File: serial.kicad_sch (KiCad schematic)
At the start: 66 parts, among them IC3 ILD217T, IC4 ILD217T, U14 NCP1117-3.3_SOT223, U15 NCP1117-3.3_SOT223, U16 SP3485EN, U17 NCP1117-3.3_SOT223, U4 ADuM1201AR, U5 ADuM1201AR, U6 ADuM1201AR, U8 SP3485EN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

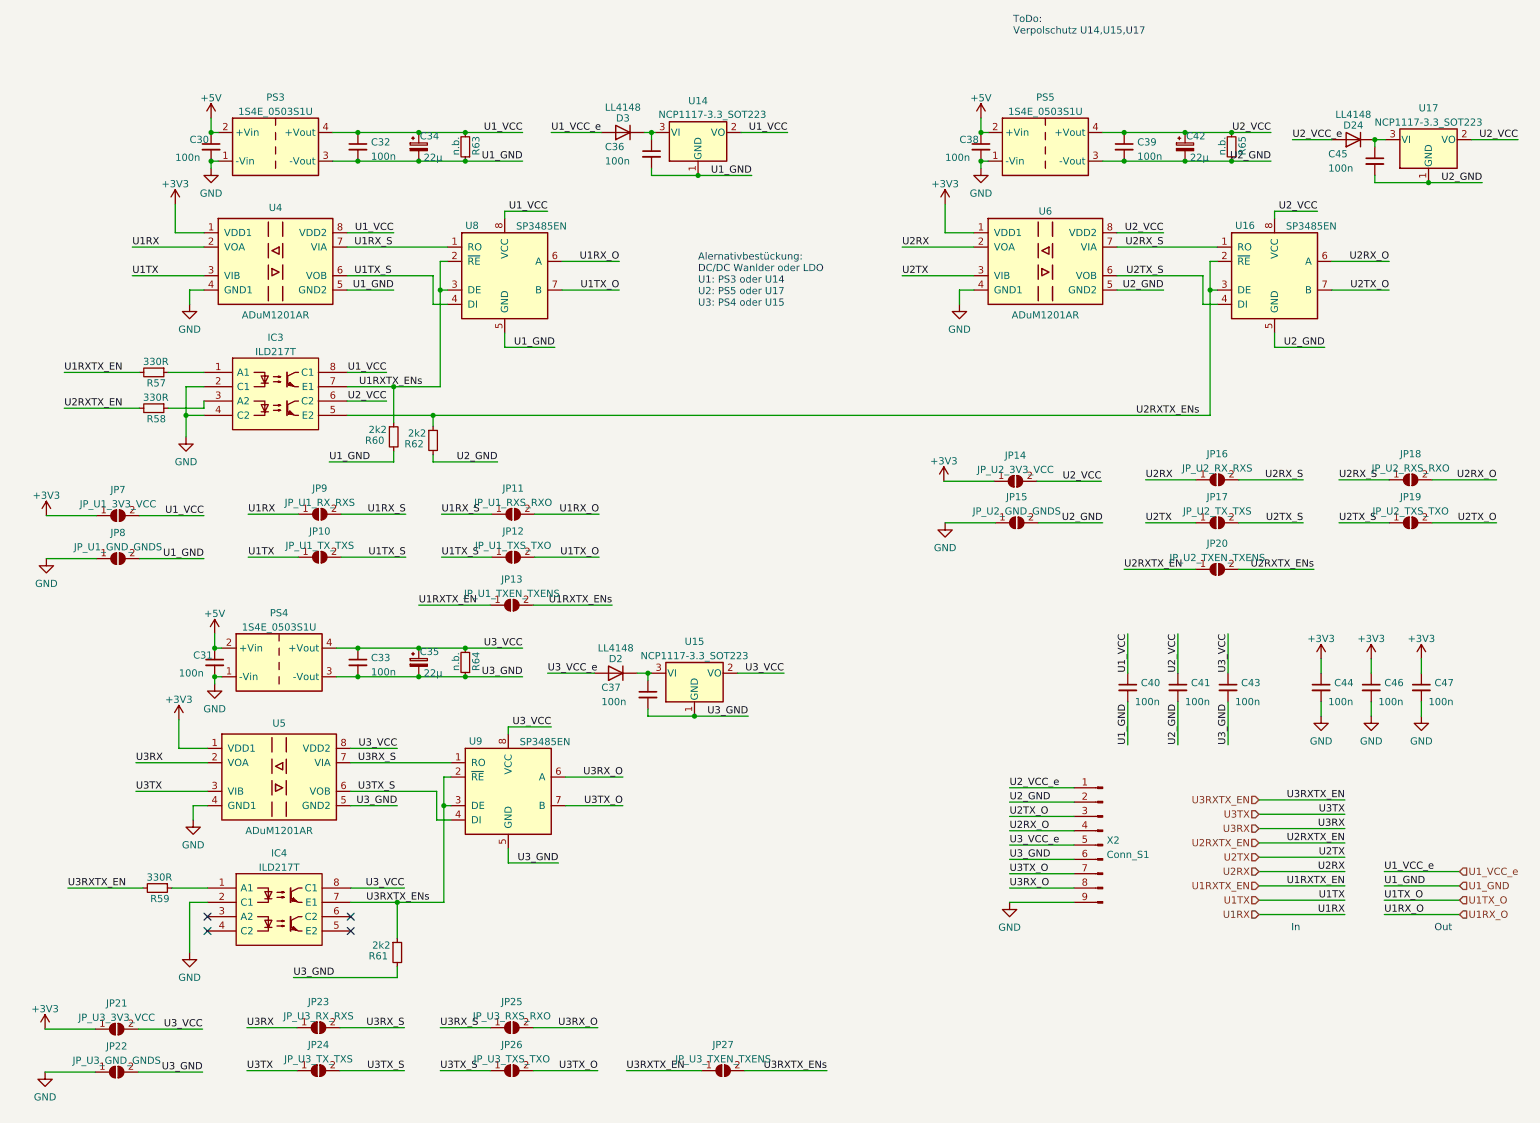
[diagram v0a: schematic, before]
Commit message: Layout optimized
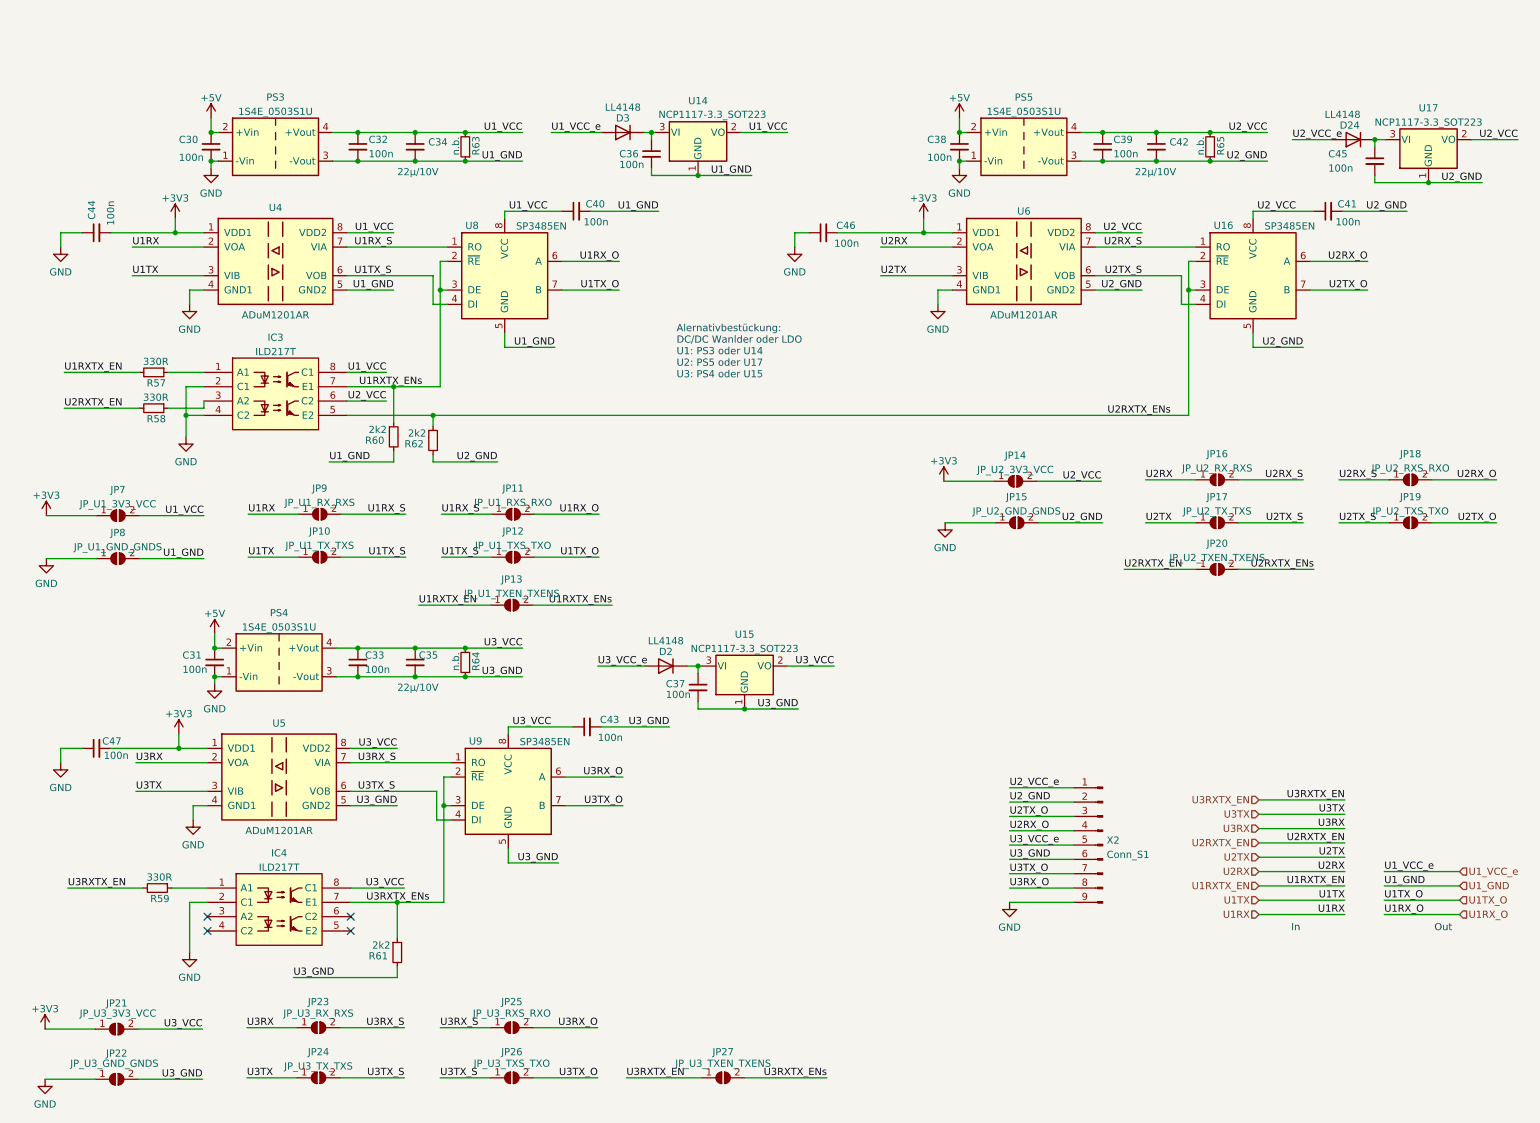
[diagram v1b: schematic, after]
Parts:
- removed C34, C35, C42: 22µ, Capacitor_SMD:CP_Elec_4x5.8, symbol Device:C_Polarized_Small
- added C34, C35, C42: 22µ/10V, Capacitor_SMD:C_1206_3216Metric, symbol Device:C_Small
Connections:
- net +3V3: now also C44.2, C46.2, C47.2; no longer C44.1, C46.1, C47.1
- net GND: now also C44.1, C46.1, C47.1; no longer C44.2, C46.2, C47.2
- net U1_GND: now also C34.2
- net U1_VCC: now also C34.1
- net U2_GND: now also C42.2
- net U2_VCC: now also C42.1
- net U3_GND: now also C35.2
- net U3_VCC: now also C35.1
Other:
- note removed: "ToDo: Verpolschutz U14,U15,U17"
- moved on the sheet: C37, C38, C39, C40, C41, C43, C44, C46, C47, D2, JP22, JP24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

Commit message: Change extension bus
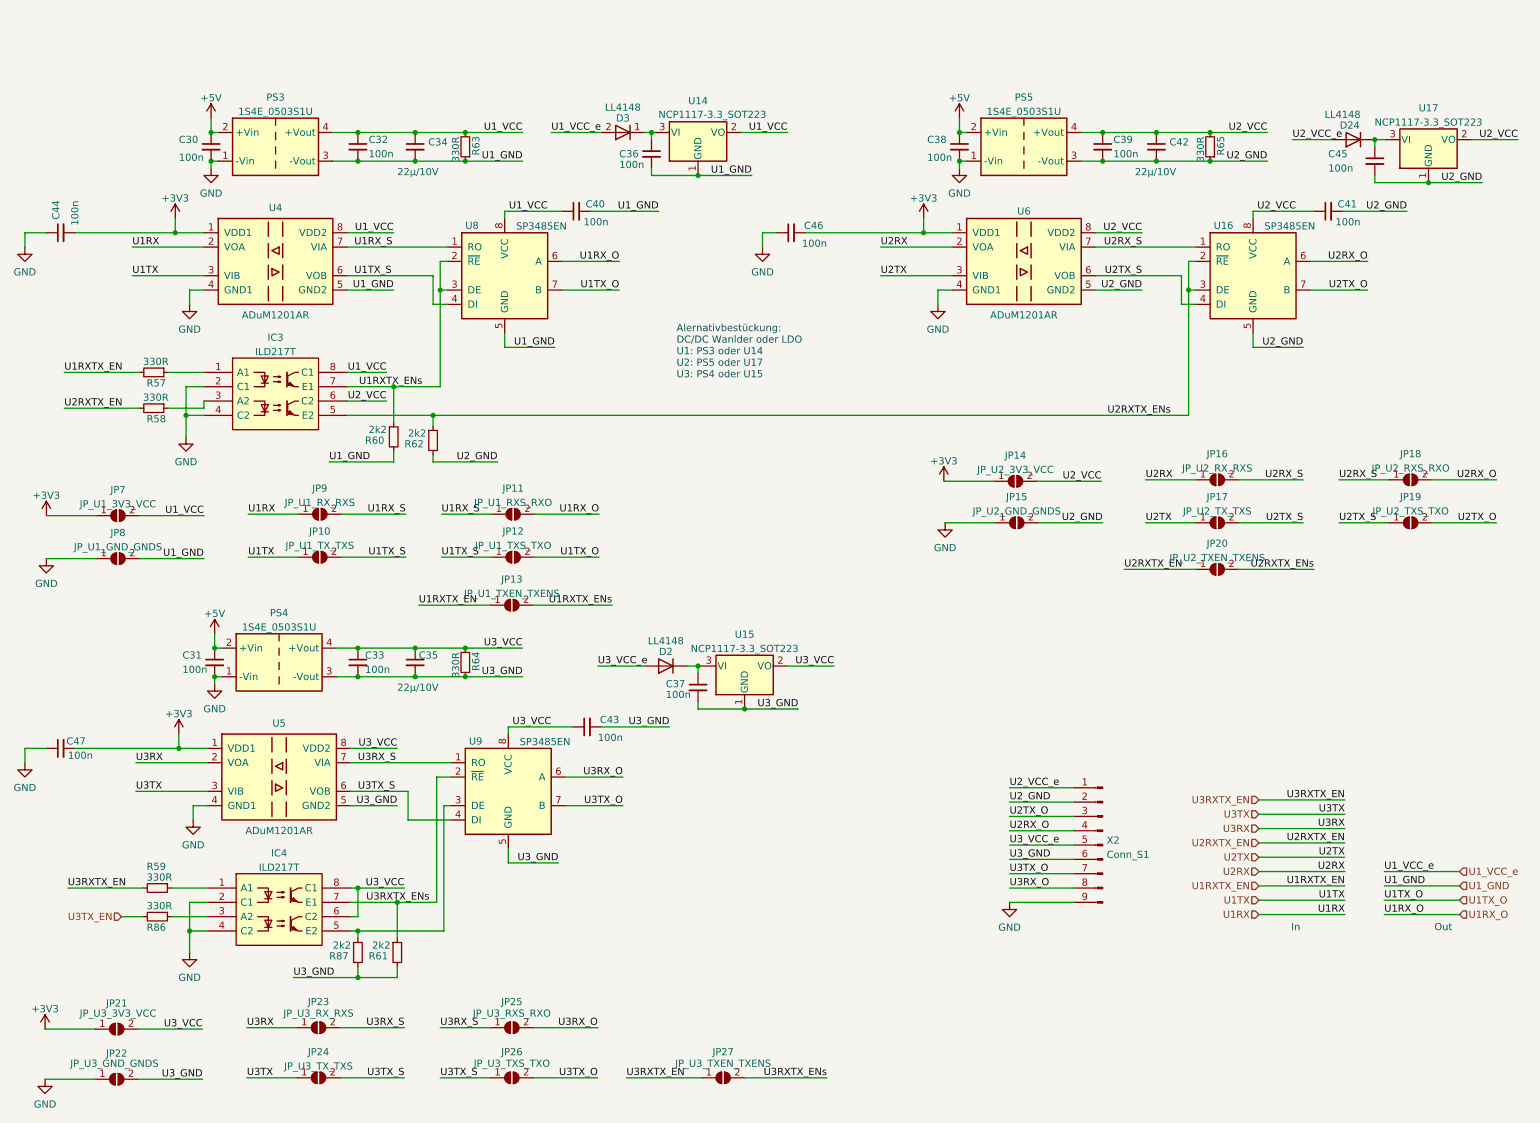
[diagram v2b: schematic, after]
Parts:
- added R86: 330R, Resistor_SMD:R_0603_1608Metric, symbol Device:R_Small
- added R87: 2k2, Resistor_SMD:R_0603_1608Metric, symbol Device:R_Small
- IC3, IC4: footprint Package_SO:SOIC-8_5.23x5.23mm_P1.27mm -> Package_SO:SOIC-8_3.9x4.9mm_P1.27mm
- R63, R64, R65: value n.b. -> 330R
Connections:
- net GND: now also IC4.4 (C2)
- net U3RXTX_ENs: no longer U9.3 (DE)
- net U3_GND: now also R87.2
- net U3_VCC: now also IC4.6 (C2)
- net at IC4.3 (A2): now also R86.1
- net at IC4.5 (E2): now also U9.3 (DE), R87.1
- new net U3TX_EN: R86.2
- no-connect marks 4 -> 0
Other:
- moved on the sheet: C44, C46, C47

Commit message: Ref 2.4
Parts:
- removed C36, C37, C45: 100n, Capacitor_SMD:C_0603_1608Metric, symbol Device:C_Small
- removed D2, D24, D3: LL4148, Diode_SMD:D_MiniMELF, symbol Diode:LL4148
- removed IC4: ILD217T, Package_SO:SOIC-8_3.9x4.9mm_P1.27mm, symbol SamacSys_Parts:ILD217T
- removed JP25: JP_U3_RXS_RXO, Jumper:SolderJumper-2_P1.3mm_Open_RoundedPad1.0x1.5mm, symbol Jumper:SolderJumper_2_Open
- removed JP26: JP_U3_TXS_TXO, Jumper:SolderJumper-2_P1.3mm_Open_RoundedPad1.0x1.5mm, symbol Jumper:SolderJumper_2_Open
- removed JP27: JP_U3_TXEN_TXENS, Jumper:SolderJumper-2_P1.3mm_Open_RoundedPad1.0x1.5mm, symbol Jumper:SolderJumper_2_Open
- removed PS3, PS4, PS5: 1S4E_0503S1U, custom_th:Converter_DCDC_GAPTEC_1S4E_S1U, symbol Converter_DCDC:MEE1S0303SC
- removed R61, R87: 2k2, Resistor_SMD:R_0603_1608Metric, symbol Device:R_Small
- removed R86: 330R, Resistor_SMD:R_0603_1608Metric, symbol Device:R_Small
- removed U14, U15, U17: NCP1117-3.3_SOT223, Package_TO_SOT_SMD:SOT-223-3_TabPin2, symbol Regulator_Linear:NCP1117-3.3_SOT223
- removed U5: ADuM1201AR, Package_SO:SOIC-8_3.9x4.9mm_P1.27mm, symbol Isolator:ADuM1201AR
- removed U9: SP3485EN, Package_SO:SOIC-8_3.9x4.9mm_P1.27mm, symbol Interface_UART:SP3485EN
- added JP32: JP_U1_120R, Jumper:SolderJumper-2_P1.3mm_Open_RoundedPad1.0x1.5mm, symbol Jumper:SolderJumper_2_Open
- added JP33: JP_U2_120R, Jumper:SolderJumper-2_P1.3mm_Open_RoundedPad1.0x1.5mm, symbol Jumper:SolderJumper_2_Open
- added JP34: JP_U3_120R, Jumper:SolderJumper-2_P1.3mm_Open_RoundedPad1.0x1.5mm, symbol Jumper:SolderJumper_2_Open
- added PS3, PS4: B0503S-1WR2, lcsc:PWRM-TH_DEXU_BXXXXS-1WR2, symbol lcsc:B0503S-1WR2_C5127059
- added PS5: (no value), symbol lcsc:B0503S-1WR2_C5127059
- added R88, R89, R90: 120R, Resistor_SMD:R_0603_1608Metric, symbol Device:R_Small
- added RJ1: R-RJ45S08P-B000, lcsc:RJ45-TH_R-RJ45S08P-B000, symbol lcsc:R-RJ45S08P-B000
- added U3: ADM2483xRW, Package_SO:SOIC-16W_7.5x10.3mm_P1.27mm, symbol Interface_UART:ADM2483xRW
- R59: value 330R -> 10k
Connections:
- net U2_VCC_e is gone; now on net U1_GND: X2.1 (Pin_1)
- net U3RX_S is gone; now on net U3RX_O: JP23.2 (B)
- net U3TX_S is gone; now on net U3TX_O: JP24.2 (B)
- net U3_VCC_e is gone; now on net U2TX_O: X2.5 (Pin_5)
- net +3V3: now also R59.2, U3.1 (VDD1)
- net +5V: now also PS3.2 (VIN), PS4.2 (VIN), PS5.2 (VIN)
- net GND: now also PS3.1 (GND), PS4.1 (GND), PS5.1 (GND), U3.2 (GND1), U3.8 (GND1); no longer X2.9 (Pin_9)
- net U1RX_O: now also X2.3 (Pin_3), R88.2
- net U1TX_O: now also X2.2 (Pin_2), JP32.2 (B)
- net U1_GND: now also PS3.3 (0V)
- net U1_VCC: now also PS3.4 (+VO)
- net U2RX_O: now also X2.6 (Pin_6), R89.2; no longer X2.4 (Pin_4)
- net U2TX_O: now also JP33.2 (B); no longer X2.3 (Pin_3)
- net U2_GND: now also X2.4 (Pin_4), PS5.3 (0V); no longer X2.2 (Pin_2)
- net U2_VCC: now also PS5.4 (+VO)
- net U3RX: now also U3.3 (RxD)
- net U3RXTX_EN: now also U3.4 (~{RE}); no longer R59.2
- net U3RX_O: now also X2.9 (Pin_9), R90.2, RJ1.2, RJ1.7, U3.12 (A); no longer X2.8 (Pin_8)
- net U3TX: now also U3.6 (TxD)
- net U3TX_EN: now also U3.5 (DE)
- net U3TX_O: now also X2.8 (Pin_8), JP34.2 (B), RJ1.1, RJ1.8, U3.13 (B); no longer X2.7 (Pin_7)
- net U3_GND: now also X2.7 (Pin_7), PS4.3 (0V), RJ1.10 (S), RJ1.3, RJ1.6, RJ1.9 (S), U3.15 (GND2), U3.9 (GND2); no longer X2.6 (Pin_6)
- net U3_VCC: now also PS4.4 (+VO), U3.16 (VDD2)
- net at R59.1: now also U3.7 (PV)
- new net: JP32.1 (A), R88.1
- new net: JP34.1 (A), R90.1
- new net: JP33.1 (A), R89.1
- no-connect marks 0 -> 2
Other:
- note removed: "Alernativbestückung: DC/DC Wanlder oder LDO U1: PS3 oder U14 U2: PS5 oder U17 U3: PS4 oder U15"
- note removed: "Out"
- moved on the sheet: C31, C32, C33, C34, C35, C39, C42, C43, C47, JP21, JP22, JP23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
